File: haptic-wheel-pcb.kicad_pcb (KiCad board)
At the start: 2 copper layers, 22 parts, among them U1 AS5600L-ASOM, U2 ESP32-C3, U3 CSD18534Q5A, U4 CSD18534Q5A, U5 CSD18534Q5A, U6 CSD18534Q5A, U7 CSD18534Q5A, U8 CSD18534Q5A, U9 DRV8323HRTAR

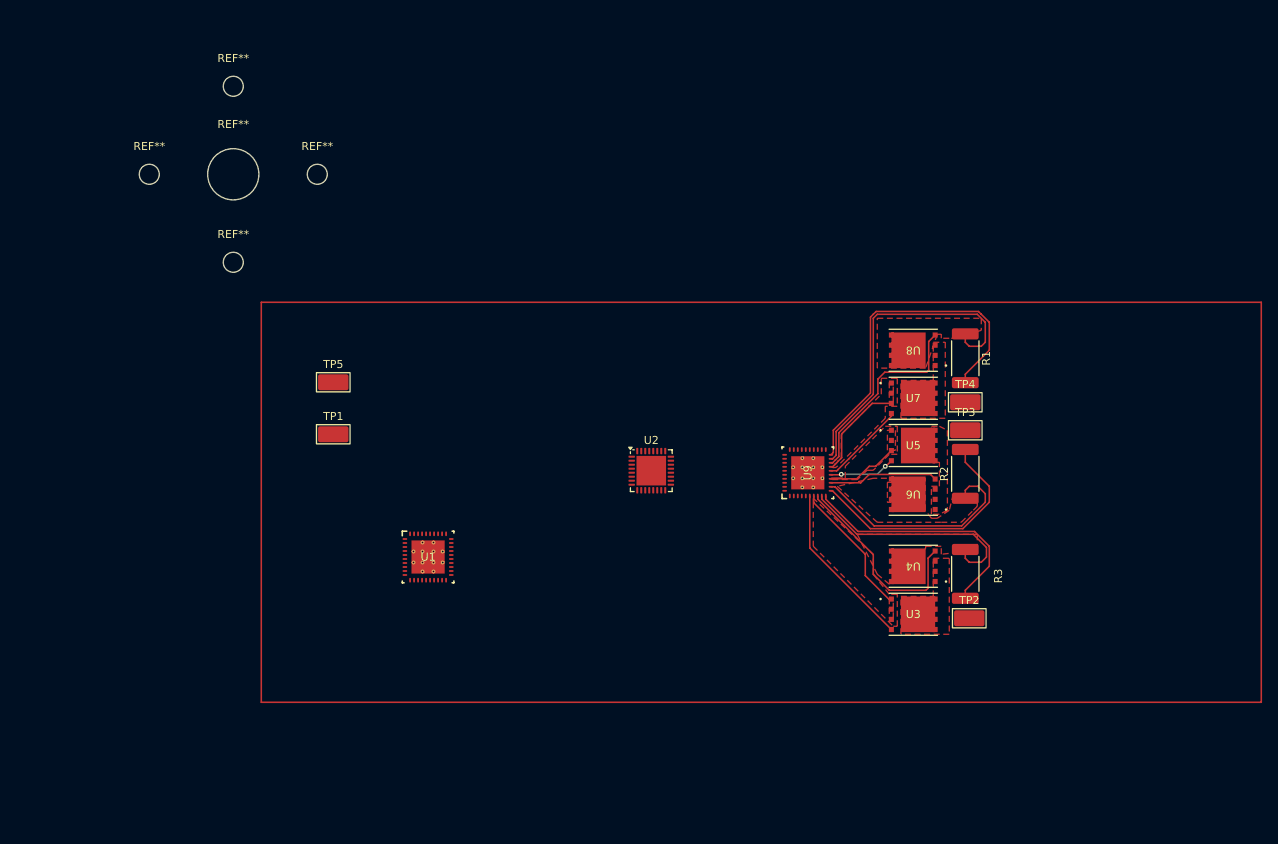
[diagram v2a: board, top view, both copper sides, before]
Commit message: using vias on SNA/SPA instead of GxA b/c switching speed
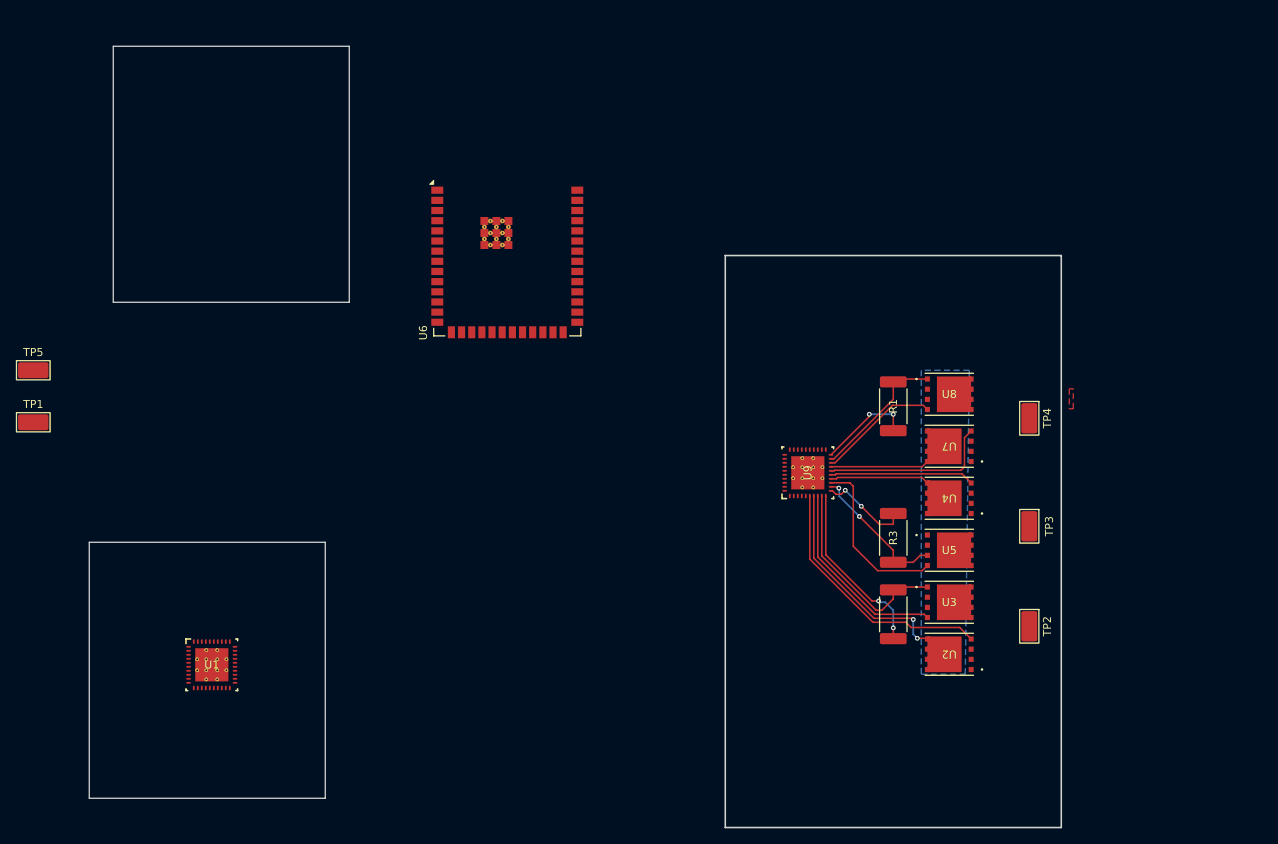
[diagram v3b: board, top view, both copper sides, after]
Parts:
- removed REF** (x4): MountingHole_2.5mm, MountingHole:MountingHole_2.5mm
- removed REF**: MountingHole_6.4mm_M6_ISO7380, MountingHole:MountingHole_6.4mm_M6_ISO7380
- U2: value ESP32-C3 -> CSD18534Q5A; footprint Package_DFN_QFN:QFN-32-1EP_5x5mm_P0.5mm_EP3.7x3.7mm -> CSD18534Q5A:DQJ8
- U6: value CSD18534Q5A -> ESP32-S3-WROOM-2; footprint CSD18534Q5A:DQJ8 -> RF_Module:ESP32-S3-WROOM-2
- moved U6 60.4 mm to (80.8, 41.2), turned to 0 degrees
- moved U2 43.8 mm to (136.0, 94.0), turned to 180 degrees
- moved TP1 37.5 mm to (21.5, 65.0)
- moved TP5 37.5 mm to (21.5, 58.5)
- moved U1 30.2 mm to (43.8, 95.3)
- moved R2 19.7 mm to (129.0, 89.0), turned to -90 degrees
- moved TP3 14.4 mm to (146.0, 78.0), turned to -90 degrees
- moved U5 13.8 mm to (136.0, 81.0)
- moved R1 10.8 mm to (129.0, 63.0)
- moved R3 10.1 mm to (129.0, 79.5), turned to 90 degrees
- moved U4 9.62 mm to (136.0, 74.5)
- moved TP4 8.25 mm to (146.0, 64.5), turned to -90 degrees
- moved TP2 7.57 mm to (146.0, 90.5), turned to -90 degrees
- moved U7 7.50 mm to (136.0, 68.0), turned to 180 degrees
- moved U8 7.11 mm to (136.0, 61.5), turned to 0 degrees
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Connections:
- net /Motor Control/M_EN renamed MOT_EN
- net /Motor Control/VCC renamed VCC
- R2 pad 1: /Motor Control/SPB -> /Motor Control/SPA
- R2 pad 2: /Motor Control/SNB -> /Motor Control/SNA
- R3 pad 1: /Motor Control/SPA -> /Motor Control/SPB
- R3 pad 2: /Motor Control/SNA -> /Motor Control/SNB
- U2 pad 1: unconnected-(U2-LNA_IN-Pad1) -> MOT_A
- U2 pad 2: Net-(U2-VDD3P3_CPU) -> MOT_A
- U2 pad 3: Net-(U2-VDD3P3_CPU) -> MOT_A
- U2 pad 4: unconnected-(U2-XTAL_32K_P-Pad4) -> Net-(U2-G)
- U2 pad 5: unconnected-(U2-XTAL_32K_N-Pad5) -> V_MOT
- U2 pad 6: IO1 -> V_MOT
- U2 pad 7: unconnected-(U2-CHIP_EN-Pad7) -> V_MOT
- U2 pad 8: IO2 -> V_MOT
- U2 pad 9: unconnected-(U2-MTMS-Pad9) -> V_MOT
- U3 pad 1: /Motor Control/SHA -> /Motor Control/SPA
- U3 pad 2: /Motor Control/SHA -> /Motor Control/SPA
- U3 pad 3: /Motor Control/SHA -> /Motor Control/SPA
- U4 pad 1: MOT_A -> MOT_B
- U4 pad 2: MOT_A -> MOT_B
- U4 pad 3: MOT_A -> MOT_B
- U4 pad 5: /Motor Control/SPA -> V_MOT
- U4 pad 6: /Motor Control/SPA -> V_MOT
- U4 pad 7: /Motor Control/SPA -> V_MOT
- U4 pad 8: /Motor Control/SPA -> V_MOT
- U4 pad 9: /Motor Control/SPA -> V_MOT
- U5 pad 1: /Motor Control/SHB -> /Motor Control/SPB
- U5 pad 2: /Motor Control/SHB -> /Motor Control/SPB
- U5 pad 3: /Motor Control/SHB -> /Motor Control/SPB
- U6 pad 1: MOT_B -> Net-(U6-GND-Pad1)
- U6 pad 2: MOT_B -> unconnected-(U6-3V3-Pad2)
- U6 pad 3: MOT_B -> unconnected-(U6-EN-Pad3)
- U6 pad 4: Net-(U6-G) -> PWM_LB
- U6 pad 5: /Motor Control/SPB -> PWM_HC
- U6 pad 6: /Motor Control/SPB -> PWM_LC
- U6 pad 7: /Motor Control/SPB -> CS
- U6 pad 8: /Motor Control/SPB -> SNSA
- U6 pad 9: /Motor Control/SPB -> SNSB
- U7 pad 1: /Motor Control/SHC -> MOT_C
- U7 pad 2: /Motor Control/SHC -> MOT_C
- U7 pad 3: /Motor Control/SHC -> MOT_C
- U7 pad 5: MOT_C -> V_MOT
- U7 pad 6: MOT_C -> V_MOT
- U7 pad 7: MOT_C -> V_MOT
- U7 pad 8: MOT_C -> V_MOT
- U7 pad 9: MOT_C -> V_MOT
- U8 pad 1: MOT_C -> /Motor Control/SPC
- U8 pad 2: MOT_C -> /Motor Control/SPC
- U8 pad 3: MOT_C -> /Motor Control/SPC
- U8 pad 5: /Motor Control/SPC -> MOT_C
- U8 pad 6: /Motor Control/SPC -> MOT_C
- U8 pad 7: /Motor Control/SPC -> MOT_C
- U8 pad 8: /Motor Control/SPC -> MOT_C
- U8 pad 9: /Motor Control/SPC -> MOT_C
- U9 pad 13: Net-(U6-G) -> Net-(U5-G)
- U9 pad 14: /Motor Control/SHB -> V_MOT
- U9 pad 15: Net-(U5-G) -> Net-(U4-G)
- U9 pad 17: /Motor Control/SHC -> V_MOT
- U9 pad 21: unconnected-(U9-SOC-Pad21) -> SNSC
- U9 pad 22: unconnected-(U9-SOB-Pad22) -> SNSB
- U9 pad 23: unconnected-(U9-SOA-Pad23) -> SNSA
- U9 pad 25: unconnected-(U9-FAULT_N-Pad25) -> Net-(U9-FAULT_N)
- U9 pad 3: unconnected-(U9-VCP-Pad3) -> Net-(U9-VCP)
- U9 pad 32: GND -> Net-(U9-AGND)
- U9 pad 34: /Motor Control/INHA -> PWM_HA
- U9 pad 35: /Motor Control/INLA -> PWM_LA
- U9 pad 36: /Motor Control/INHB -> PWM_HB
- U9 pad 37: /Motor Control/INLB -> PWM_LB
- U9 pad 38: /Motor Control/INHC -> PWM_HC
- U9 pad 39: /Motor Control/INLC -> PWM_LC
- U9 pad 4: unconnected-(U9-VM-Pad4) -> Net-(U9-VM)
- U9 pad 5: unconnected-(U9-VDRAIN-Pad5) -> V_MOT
- U9 pad 6: Net-(U3-G) -> Net-(U2-G)
- U9 pad 7: /Motor Control/SHA -> V_MOT
- U9 pad 8: Net-(U4-G) -> Net-(U3-G)
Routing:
- net V_MOT: track 0.00 -> 52.0 mm, vias 0 -> 2
- net /Motor Control/SNC: track 44.8 -> 12.1 mm, vias 0 -> 2
- net Net-(U2-G): track 0.00 -> 32.2 mm
- net /Motor Control/SPC: track 42.0 -> 17.5 mm
- net /Motor Control/SNB: track 31.0 -> 11.3 mm, vias 0 -> 2
- net /Motor Control/SHA: track 17.1 -> 0.00 mm
- net Net-(U6-G): track 13.7 -> 0.00 mm
- net Net-(U5-G): track 8.28 -> 21.3 mm, vias 2 -> 0
- net /Motor Control/SHC: track 12.6 -> 0.00 mm
- net Net-(U7-G): track 10.7 -> 21.7 mm
- net /Motor Control/SPB: track 27.7 -> 17.8 mm, vias 0 -> 2
- net Net-(U8-G): track 24.5 -> 15.2 mm
- net /Motor Control/SHB: track 9.01 -> 0.00 mm
- net /Motor Control/SNA: track 31.0 -> 22.2 mm, vias 0 -> 2
- net Net-(U4-G): track 25.5 -> 18.0 mm
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- added copper zone on B.Cu, net V_MOT
- added copper zone on F.Cu, net V_MOT
- removed copper zone on F.Cu, net /Motor Control/SHA
- removed copper zone on F.Cu, net /Motor Control/SHB
- removed copper zone on F.Cu, net /Motor Control/SHC
- removed copper zone on F.Cu, net /Motor Control/SPA
- removed copper zone on F.Cu, net /Motor Control/SPB
- removed copper zone on F.Cu, net /Motor Control/SPC
- removed copper zone on F.Cu, net MOT_A
- removed copper zone on F.Cu, net MOT_B
- removed copper zone on F.Cu, net MOT_C
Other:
- board outline added: 121.5 x 97.7 mm

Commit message: full gate reroute with zones and sense lines like the layout guide
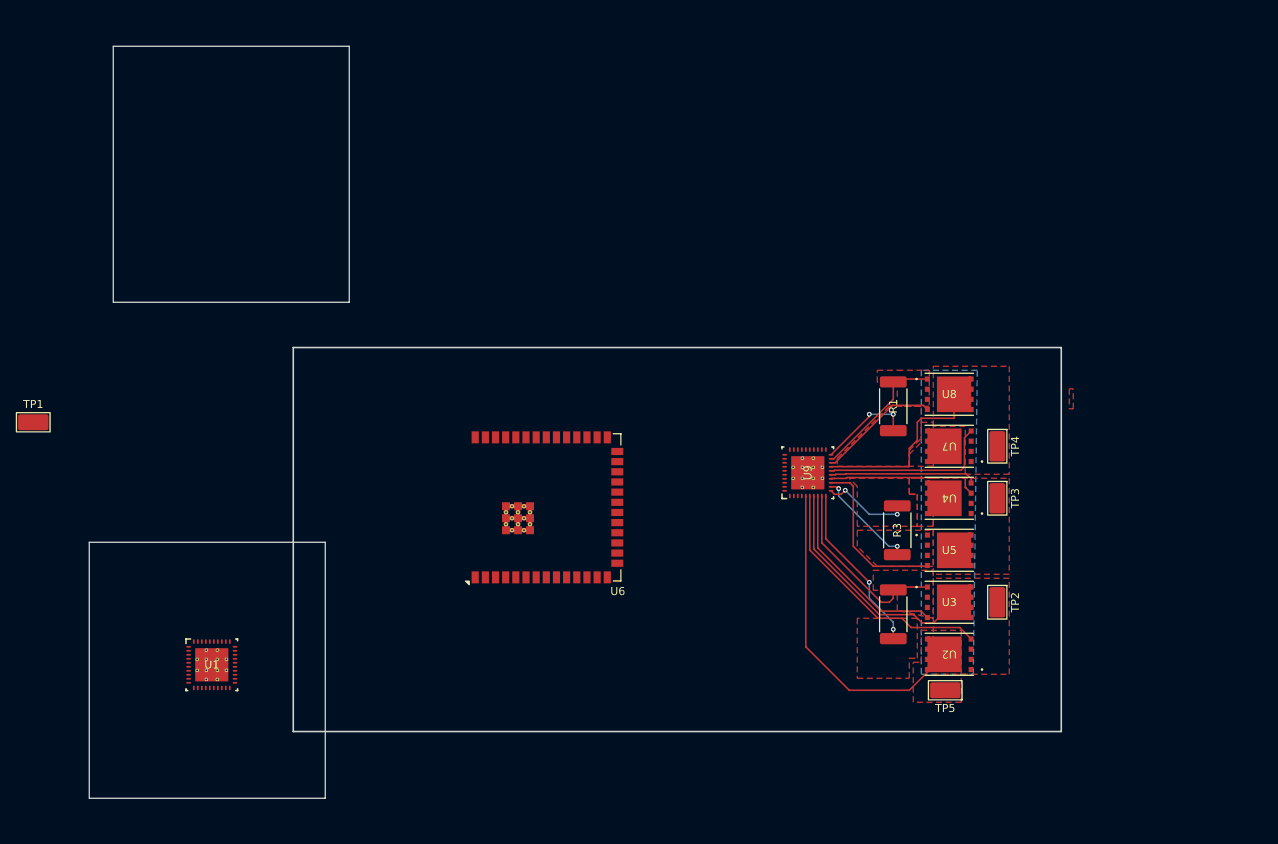
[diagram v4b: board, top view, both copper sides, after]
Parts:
- moved TP5 120.8 mm to (135.5, 98.5), turned to 180 degrees
- moved U6 34.4 mm to (82.0, 75.6), turned to 90 degrees
- moved TP3 5.32 mm to (142.0, 74.5)
- moved TP4 5.32 mm to (142.0, 68.0)
- moved TP2 5.00 mm to (142.0, 87.5)
- moved R3 1.07 mm to (129.5, 78.5)
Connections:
- U9 pad 14: V_MOT -> MOT_B
- U9 pad 17: V_MOT -> MOT_C
- U9 pad 7: V_MOT -> MOT_A
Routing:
- net MOT_A: track 0.00 -> 29.1 mm
- net MOT_C: track 0.00 -> 23.5 mm
- net MOT_B: track 0.00 -> 19.1 mm
- net V_MOT: track 52.0 -> 37.6 mm, vias 2 -> 0
- net /Motor Control/SPB: track 17.8 -> 13.0 mm
- net /Motor Control/SPA: track 25.4 -> 23.5 mm
- net /Motor Control/SNB: track 11.3 -> 9.92 mm
- net /Motor Control/SNA: track 22.2 -> 21.3 mm
- net Net-(U2-G): track 32.2 -> 31.5 mm
- net Net-(U3-G): track 24.5 -> 23.8 mm
- added copper zone on F.Cu, net /Motor Control/SNA
- added copper zone on F.Cu, net /Motor Control/SNB
- added copper zone on F.Cu, net /Motor Control/SNC
- added copper zone on F.Cu, net /Motor Control/SPA
- added copper zone on F.Cu, net /Motor Control/SPB
- added copper zone on F.Cu, net /Motor Control/SPC
- added copper zone on F.Cu, net MOT_A
- added copper zone on F.Cu, net MOT_B
- added copper zone on F.Cu, net MOT_C
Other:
- board size 121.5 x 97.7 mm -> 121.5 x 94 mm

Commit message: selected mcu pins for sense in, SPI
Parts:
- removed U1: AS5600L-ASOM, DRV8323:RTA0040B
- added J1: Screw_Terminal_01x02, TerminalBlock:TerminalBlock_Xinya_XY308-2.54-2P_1x02_P2.54mm_Horizontal, F.Cu at (116.5, 99.5)
- added J2: Screw_Terminal_01x02, TerminalBlock:TerminalBlock_Xinya_XY308-2.54-2P_1x02_P2.54mm_Horizontal, F.Cu at (119.0, 59.5)
- added J3: Screw_Terminal_01x03, TerminalBlock:TerminalBlock_Xinya_XY308-2.54-3P_1x03_P2.54mm_Horizontal, F.Cu at (148.7, 79.5)
- added TP10: TestPoint, TestPoint:TestPoint_Keystone_5019_Miniature, F.Cu at (79.5, 22.2)
- added TP11: TestPoint, TestPoint:TestPoint_Keystone_5019_Miniature, F.Cu at (79.5, 26.1)
- added TP12: TestPoint, TestPoint:TestPoint_Keystone_5019_Miniature, F.Cu at (85.3, 18.2)
- added TP13: TestPoint, TestPoint:TestPoint_Keystone_5019_Miniature, F.Cu at (85.3, 22.2)
- added TP14: TestPoint, TestPoint:TestPoint_Keystone_5019_Miniature, F.Cu at (85.3, 26.1)
- added TP6: TestPoint, TestPoint:TestPoint_Keystone_5019_Miniature, F.Cu at (73.8, 18.2)
- added TP7: TestPoint, TestPoint:TestPoint_Keystone_5019_Miniature, F.Cu at (73.8, 22.2)
- added TP8: TestPoint, TestPoint:TestPoint_Keystone_5019_Miniature, F.Cu at (73.8, 26.1)
- added TP9: TestPoint, TestPoint:TestPoint_Keystone_5019_Miniature, F.Cu at (79.5, 18.2)
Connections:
- TP1 pad 1: unconnected-(TP1-Pad1) -> VCC
- U6 pad 10: SNSC -> unconnected-(U6-IO17-Pad10)
- U6 pad 12: CLK -> unconnected-(U6-IO8-Pad12)
- U6 pad 15: PWM_HB -> PWM_LC
- U6 pad 16: unconnected-(U6-IO46-Pad16) -> PWM_HC
- U6 pad 17: MISO -> PWM_LB
- U6 pad 18: MOSI -> PWM_HB
- U6 pad 19: SCL -> PWM_LA
- U6 pad 20: SDA -> PWM_HA
- U6 pad 21: unconnected-(U6-IO13-Pad21) -> MOT_EN
- U6 pad 24: unconnected-(U6-IO47-Pad24) -> SNSA
- U6 pad 25: unconnected-(U6-IO48-Pad25) -> SNSB
- U6 pad 26: unconnected-(U6-IO45-Pad26) -> SNSC
- U6 pad 31: unconnected-(U6-IO38-Pad31) -> CS
- U6 pad 32: unconnected-(U6-MTCK/IO39-Pad32) -> CLK
- U6 pad 33: unconnected-(U6-MTDO/IO40-Pad33) -> MOSI
- U6 pad 34: unconnected-(U6-MTDI/IO41-Pad34) -> MISO
- U6 pad 38: PWM_LA -> unconnected-(U6-IO2-Pad38)
- U6 pad 39: PWM_HA -> unconnected-(U6-IO1-Pad39)
- U6 pad 4: PWM_LB -> unconnected-(U6-IO4-Pad4)
- U6 pad 5: PWM_HC -> unconnected-(U6-IO5-Pad5)
- U6 pad 6: PWM_LC -> unconnected-(U6-IO6-Pad6)
- U6 pad 7: CS -> unconnected-(U6-IO7-Pad7)
- U6 pad 8: SNSA -> unconnected-(U6-IO15-Pad8)
- U6 pad 9: SNSB -> unconnected-(U6-IO16-Pad9)
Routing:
- net MOT_A: track 29.1 -> 39.7 mm
- net MOT_C: track 23.5 -> 32.7 mm
- net MOT_B: track 19.1 -> 26.6 mm
- net V_MOT: track 37.6 -> 42.5 mm
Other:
- board size 121.5 x 94 mm -> 124 x 94 mm

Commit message: big layout - lay pgnd and agnd zones and add SPI header pins
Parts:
- added C1: 47 nF, Capacitor_SMD:C_0805_2012Metric_Pad1.18x1.45mm_HandSolder, F.Cu at (46.0, 29.9)
- added C10: C, Capacitor_SMD:C_0805_2012Metric_Pad1.18x1.45mm_HandSolder, F.Cu at (130.5, 69.0)
- added C2: 1 uF, Capacitor_SMD:C_0805_2012Metric_Pad1.18x1.45mm_HandSolder, F.Cu at (46.0, 32.9)
- added C3: 0.1 uF, Capacitor_SMD:C_0805_2012Metric_Pad1.18x1.45mm_HandSolder, F.Cu at (46.0, 36.0)
- added C4: C, Capacitor_SMD:C_0805_2012Metric_Pad1.18x1.45mm_HandSolder, F.Cu at (57.5, 29.9)
- added C5: 1 uF, Capacitor_SMD:C_0805_2012Metric_Pad1.18x1.45mm_HandSolder, F.Cu at (46.0, 39.0)
- added C6: 0.1 uF, Capacitor_SMD:C_0805_2012Metric_Pad1.18x1.45mm_HandSolder, F.Cu at (56.0, 42.5)
- added C8: C, Capacitor_SMD:C_0805_2012Metric_Pad1.18x1.45mm_HandSolder, F.Cu at (130.5, 95.0)
- added C9: C, Capacitor_SMD:C_0805_2012Metric_Pad1.18x1.45mm_HandSolder, F.Cu at (130.5, 73.0)
- added J4: Conn_01x04_Pin, Connector_PinHeader_2.54mm:PinHeader_1x04_P2.54mm_Vertical, F.Cu at (102.2, 68.0)
- added R4: R_US, Resistor_SMD:R_0805_2012Metric_Pad1.20x1.40mm_HandSolder, F.Cu at (50.7, 29.9)
- TP1, TP10, TP11, TP12, TP13, TP14, TP2, TP3, TP4, TP5, TP6, TP7, TP8, TP9: footprint TestPoint:TestPoint_Keystone_5019_Miniature -> TestPoint:TestPoint_Keystone_5015_Micro_Mini
- moved TP1 90.9 mm to (112.2, 60.5)
- moved TP12 63.4 mm to (99.8, 80.0)
- moved TP9 62.8 mm to (104.2, 76.0)
- moved TP13 62.3 mm to (104.2, 81.5)
- moved TP10 58.9 mm to (99.8, 77.5)
- moved TP14 58.4 mm to (99.8, 82.8)
- moved TP11 58.1 mm to (104.2, 78.8)
- moved TP2 5.48 mm to (146.0, 83.8)
- moved TP4 3.55 mm to (144.8, 70.2)
- moved TP6 3.53 mm to (77.2, 17.5)
- moved TP7 3.53 mm to (77.2, 21.4)
- moved TP8 3.53 mm to (77.2, 25.4)
- moved TP3 3.13 mm to (143.5, 77.2)
- moved R3 0.50 mm to (129.0, 78.5)
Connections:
- J1 pad 1: GND -> PGND
- J2 pad 1: GND -> AGND
- U6 pad 22: unconnected-(U6-IO14-Pad22) -> SPI_CS
- U6 pad 23: unconnected-(U6-IO21-Pad23) -> SPI_CLK
- U6 pad 24: SNSA -> SPI_MOSI
- U6 pad 25: SNSB -> SPI_MISO
- U6 pad 26: SNSC -> unconnected-(U6-IO45-Pad26)
- U6 pad 31: CS -> NFLT
- U6 pad 32: CLK -> SNSA
- U6 pad 33: MOSI -> SNSB
- U6 pad 34: MISO -> SNSC
- U9 pad 25: Net-(U9-FAULT_N) -> NFLT
- U9 pad 26: unconnected-(U9-MODE_SDO-Pad26) -> SPI_MISO
- U9 pad 27: unconnected-(U9-IDRIVE_SDI-Pad27) -> SPI_MOSI
- U9 pad 28: unconnected-(U9-VDS_SCLK-Pad28) -> SPI_CLK
- U9 pad 29: unconnected-(U9-GAIN_SCS_N-Pad29) -> SPI_CS
- U9 pad 32: Net-(U9-AGND) -> AGND
- U9 pad 40: GND -> PGND
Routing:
- net SNSC: track 0.00 -> 42.1 mm, vias 0 -> 2
- net SNSB: track 0.00 -> 39.7 mm, vias 0 -> 2
- net SNSA: track 0.00 -> 37.3 mm, vias 0 -> 2
- net NFLT: track 0.00 -> 33.5 mm
- net V_MOT: track 42.5 -> 11.3 mm
- net SPI_MISO: track 0.00 -> 26.9 mm
- net SPI_MOSI: track 0.00 -> 26.3 mm
- net SPI_CLK: track 0.00 -> 25.9 mm
- net PWM_LC: track 0.00 -> 25.9 mm
- net SPI_CS: track 0.00 -> 25.1 mm
- net PWM_HC: track 0.00 -> 24.6 mm
- net MOT_EN: track 0.00 -> 24.3 mm
- net PWM_LB: track 0.00 -> 24.2 mm
- net PWM_HB: track 0.00 -> 23.9 mm
- net PWM_LA: track 0.00 -> 23.6 mm
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- added copper zone on B.Cu, net AGND
- added copper zone on F.Cu, net AGND
- added copper zone on B.Cu, net PGND
- added copper zone on F.Cu, net PGND
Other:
- board size 124 x 94 mm -> 98.5 x 48 mm
